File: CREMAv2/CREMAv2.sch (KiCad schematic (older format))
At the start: 19 parts, among them IC1 ADS124S06IPBSR, J1 SPI, J2 RTD1, J3 RTD2

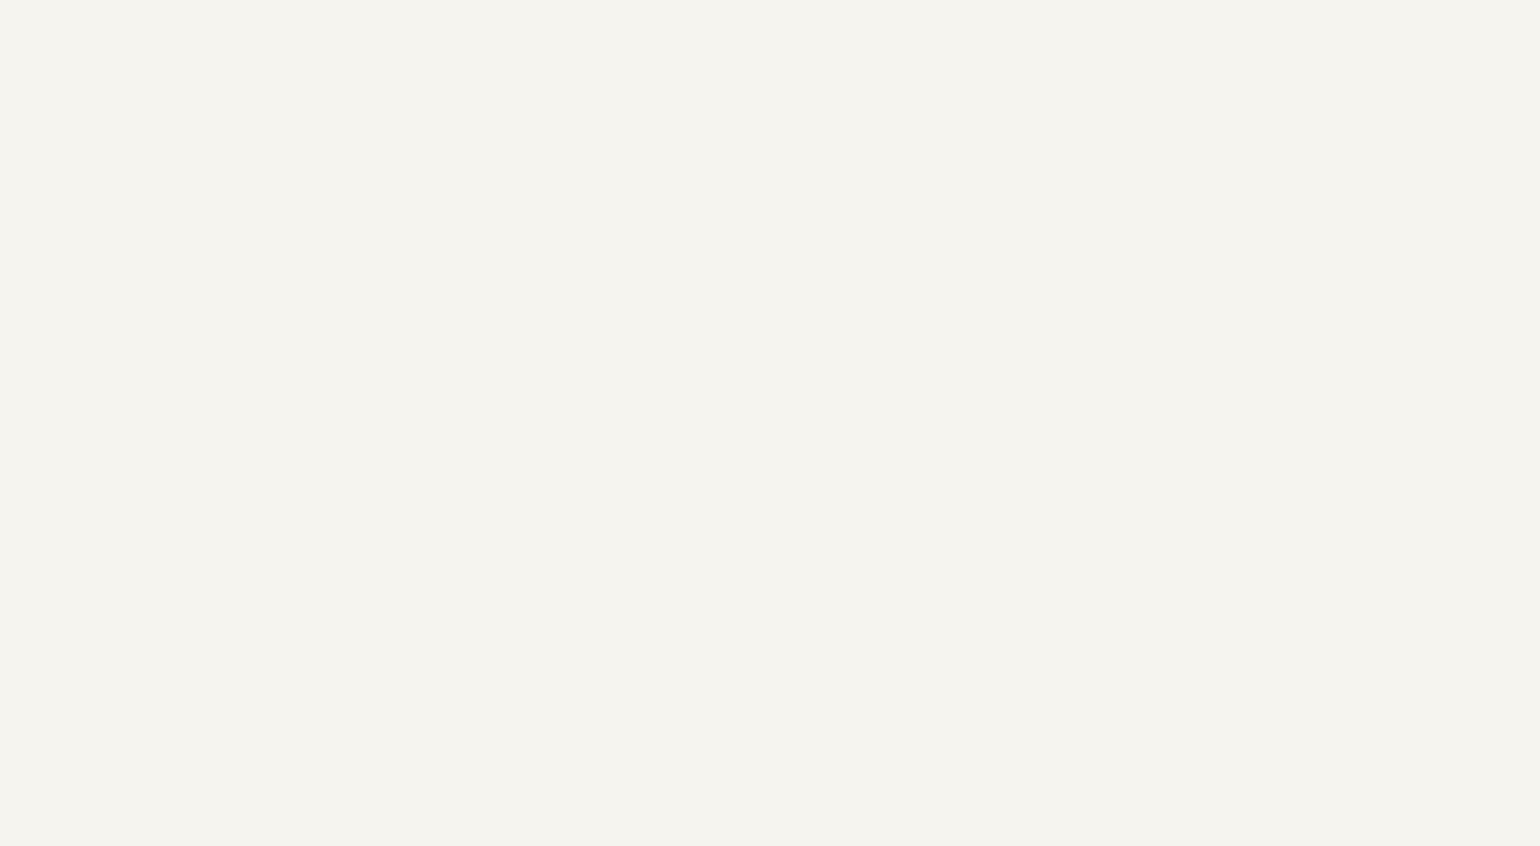
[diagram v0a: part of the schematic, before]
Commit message: Added power to the schematic. Updated PDFs. Added KiCad symbols.
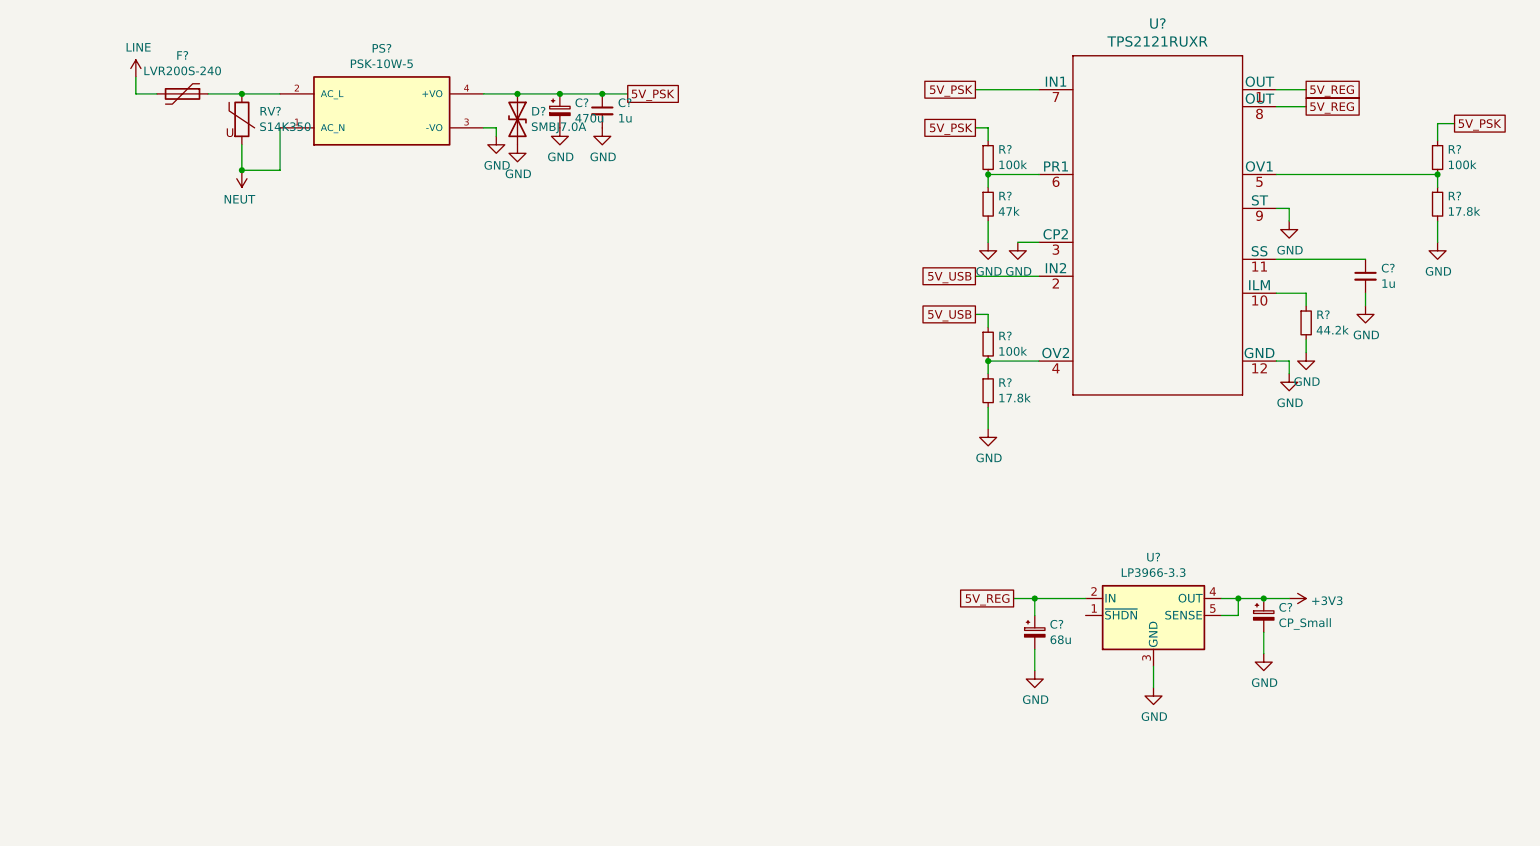
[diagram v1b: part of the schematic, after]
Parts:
- added C?: 470u, symbol Device:CP_Small
- added C? (x2): 1u, symbol Device:C_Small
- added C?: 68u, symbol Device:CP_Small
- added C?: CP_Small, symbol Device:CP_Small
- added D?: SMBJ7.0A, symbol Device:D_TVS
- added F?: LVR200S-240, symbol Device:Polyfuse
- added PS?: PSK-10W-5, CONV_PSK-10W-5, symbol PSK-10W:PSK-10W-5
- added R? (x3): 100k, symbol Device:R_Small
- added R?: 47k, symbol Device:R_Small
- added R? (x2): 17.8k, symbol Device:R_Small
- added R?: 44.2k, symbol Device:R_Small
- added RV?: S14K350, symbol Device:Varistor
- added U?: TPS2121RUXR, RUX0012A, symbol TPS2121:TPS2121RUXR
- added U?: LP3966-3.3, symbol Regulator_Linear:LP3966-3.3
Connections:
- net +3V3: now also C?.1, U?.4 (OUT), U?.5 (SENSE)
- net GND: now also C?.2, C?.2, C?.2, C?.2, C?.2, D?.2 (A2), PS?.3 (-VO), R?.2, R?.2, R?.2, R?.2, U?.12 (GND), U?.3 (CP2), U?.3 (GND), U?.9 (ST)
- new net: F?.1, PS?.2 (AC_L), RV?.1
- new net: R?.1, U?.10 (ILM)
- new net: C?.1, U?.11 (SS)
- new net: R?.1, R?.2, U?.4 (OV2)
- new net: R?.1, R?.2, U?.5 (OV1)
- new net: R?.1, R?.2, U?.6 (PR1)
- new net 5V_PSK: C?.1, C?.1, D?.1 (A1), PS?.4 (+VO), R?.1, R?.1, U?.7 (IN1)
- new net 5V_REG: C?.1, U?.1 (OUT), U?.2 (IN), U?.8 (OUT)
- new net 5V_USB: R?.1, U?.2 (IN2)
- new net LINE: F?.2
- new net NEUT: PS?.1 (AC_N), RV?.2
